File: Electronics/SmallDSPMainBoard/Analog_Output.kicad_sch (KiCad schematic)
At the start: 57 parts, among them J13 NC3MAAH, J14 NC3MAAH

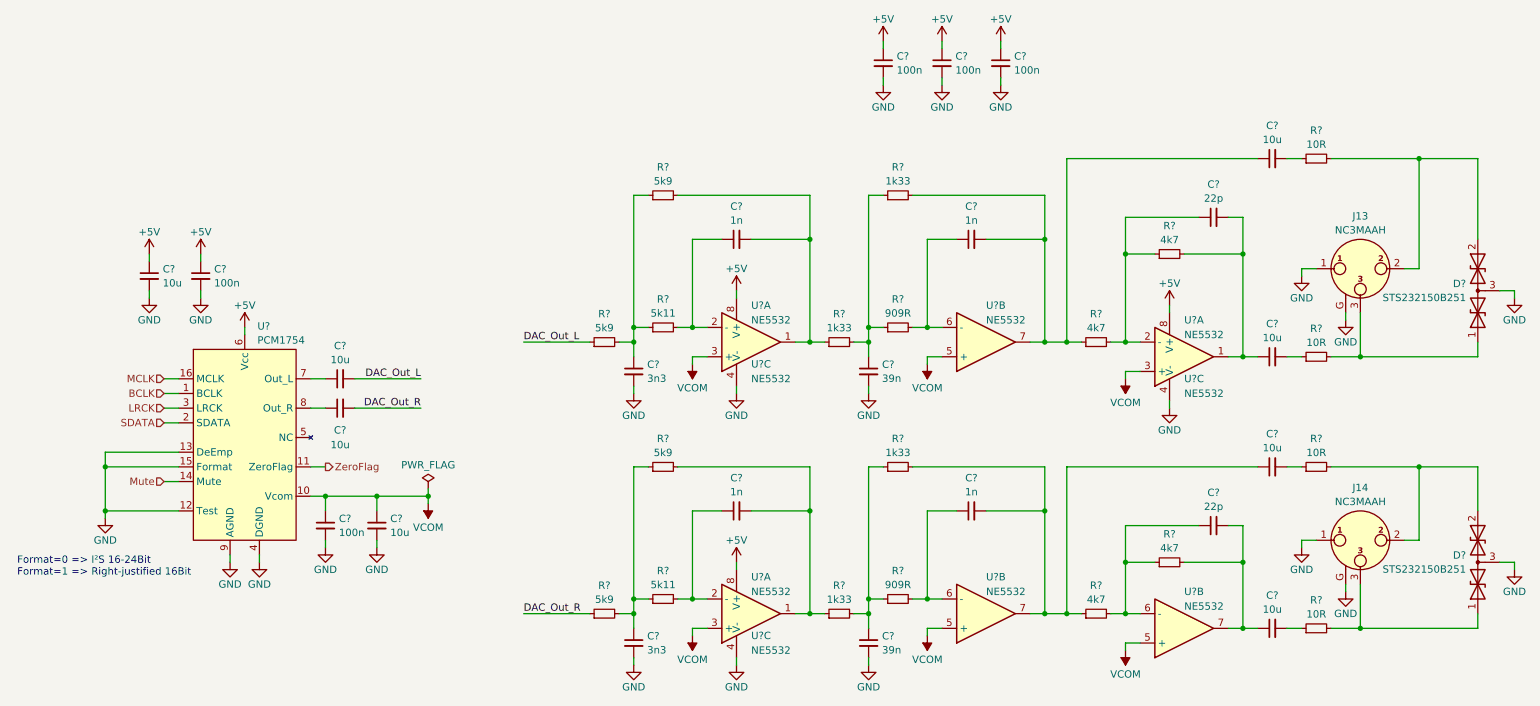
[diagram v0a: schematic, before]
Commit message: Partly finishes layout
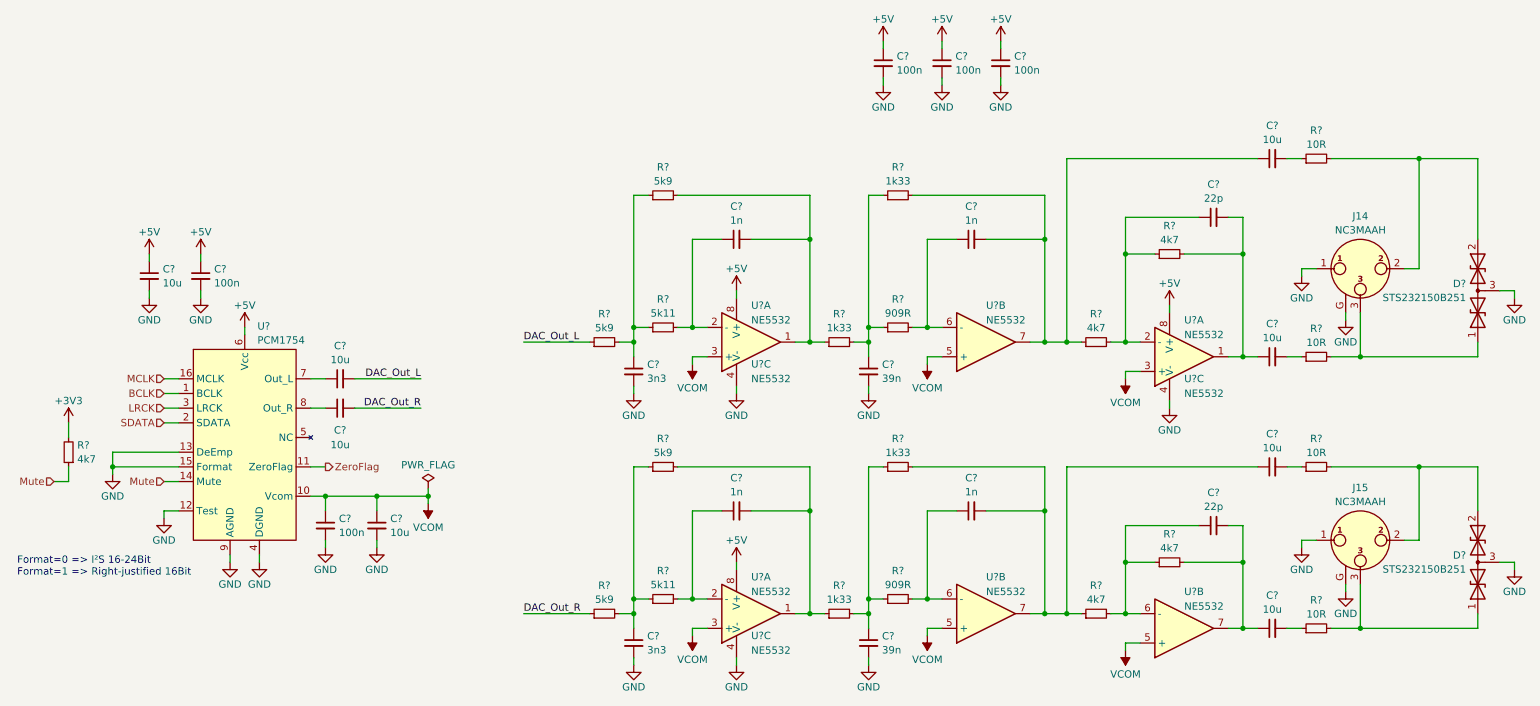
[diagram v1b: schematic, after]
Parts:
- added R?: 4k7, Resistor_SMD:R_0402_1005Metric, symbol Device:R_Small
- renumbered J13 to J14, J14 to J15
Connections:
- net Mute: now also R?.1
- new net +3V3: R?.2

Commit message: Finishes layout of Rev 1.0 and fixes a polarity error in the schematic
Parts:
- U?: Part Number PCM1754 -> PCM1754DBQR
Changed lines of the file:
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@@
       (effects (font (size 1.27 1.27)) hide)
     )
-    (property "Datasheet" "https://fscdn.rohm.com/en/products/databook/datasheet/ic/amp_linear/opamp/lm4565f-e.pdf" (at 186.69 129.54 0)
+    (property "Datasheet" "~" (at 186.69 129.54 0)
       (effects (font (size 1.27 1.27)) hide)
     )
@@
       (effects (font (size 1.27 1.27)) hide)
     )
-    (property "Datasheet" "https://fscdn.rohm.com/en/products/databook/datasheet/ic/amp_linear/opamp/lm4565f-e.pdf" (at 146.05 129.54 0)
+    (property "Datasheet" "~" (at 146.05 129.54 0)
       (effects (font (size 1.27 1.27)) hide)
     )
@@
       (effects (font (size 1.27 1.27)) hide)
     )
-    (property "Datasheet" "https://fscdn.rohm.com/en/products/databook/datasheet/ic/amp_linear/opamp/lm4565f-e.pdf" (at 146.05 82.55 0)
+    (property "Datasheet" "~" (at 146.05 82.55 0)
       (effects (font (size 1.27 1.27)) hide)
     )
@@
       (effects (font (size 1.27 1.27)) hide)
     )
-    (property "Datasheet" "https://fscdn.rohm.com/en/products/databook/datasheet/ic/amp_linear/opamp/lm4565f-e.pdf" (at 186.69 82.55 0)
+    (property "Datasheet" "~" (at 186.69 82.55 0)
       (effects (font (size 1.27 1.27)) hide)
     )
@@
       (effects (font (size 1.27 1.27)) hide)
     )
-    (property "Datasheet" "https://fscdn.rohm.com/en/products/databook/datasheet/ic/amp_linear/opamp/lm4565f-e.pdf" (at 220.98 85.09 0)
+    (property "Datasheet" "~" (at 220.98 85.09 0)
       (effects (font (size 1.27 1.27)) hide)
     )
@@
       (effects (font (size 1.27 1.27)) hide)
     )
-    (property "Datasheet" "https://fscdn.rohm.com/en/products/databook/datasheet/ic/amp_linear/opamp/lm4565f-e.pdf" (at 220.98 132.08 0)
+    (property "Datasheet" "~" (at 220.98 132.08 0)
       (effects (font (size 1.27 1.27)) hide)
     )
@@
         )
         (path "/5f2729b5-edcd-4fbc-b3fb-44096724c941/55a5d435-d0ac-41f8-8f25-907deabbd2ff"
-          (reference "#FLG05") (unit 1)
+          (reference "#FLG02") (unit 1)
         )
       )
@@
       (effects (font (size 1.27 1.27)) hide)
     )
-    (property "Datasheet" "https://fscdn.rohm.com/en/products/databook/datasheet/ic/amp_linear/opamp/lm4565f-e.pdf" (at 146.05 129.54 0)
+    (property "Datasheet" "~" (at 146.05 129.54 0)
       (effects (font (size 1.27 1.27)) hide)
     )
@@
       (effects (font (size 1.27 1.27)) hide)
     )
-    (property "Part Number" "PCM1754" (at 58.42 64.77 0)
+    (property "Part Number" "PCM1754DBQR" (at 58.42 64.77 0)
       (effects (font (size 1.27 1.27)) hide)
     )
@@
       (effects (font (size 1.27 1.27)) hide)
     )
-    (property "Datasheet" "https://fscdn.rohm.com/en/products/databook/datasheet/ic/amp_linear/opamp/lm4565f-e.pdf" (at 220.98 85.09 0)
+    (property "Datasheet" "~" (at 220.98 85.09 0)
       (effects (font (size 1.27 1.27)) hide)
     )
@@
       (effects (font (size 1.27 1.27)) hide)
     )
-    (property "Datasheet" "https://fscdn.rohm.com/en/products/databook/datasheet/ic/amp_linear/opamp/lm4565f-e.pdf" (at 146.05 82.55 0)
+    (property "Datasheet" "~" (at 146.05 82.55 0)
       (effects (font (size 1.27 1.27)) hide)
     )
